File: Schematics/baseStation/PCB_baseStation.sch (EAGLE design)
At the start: 9 parts, among them U1 ATMEGA328P, U2 MCP1824ST-3302E/DB

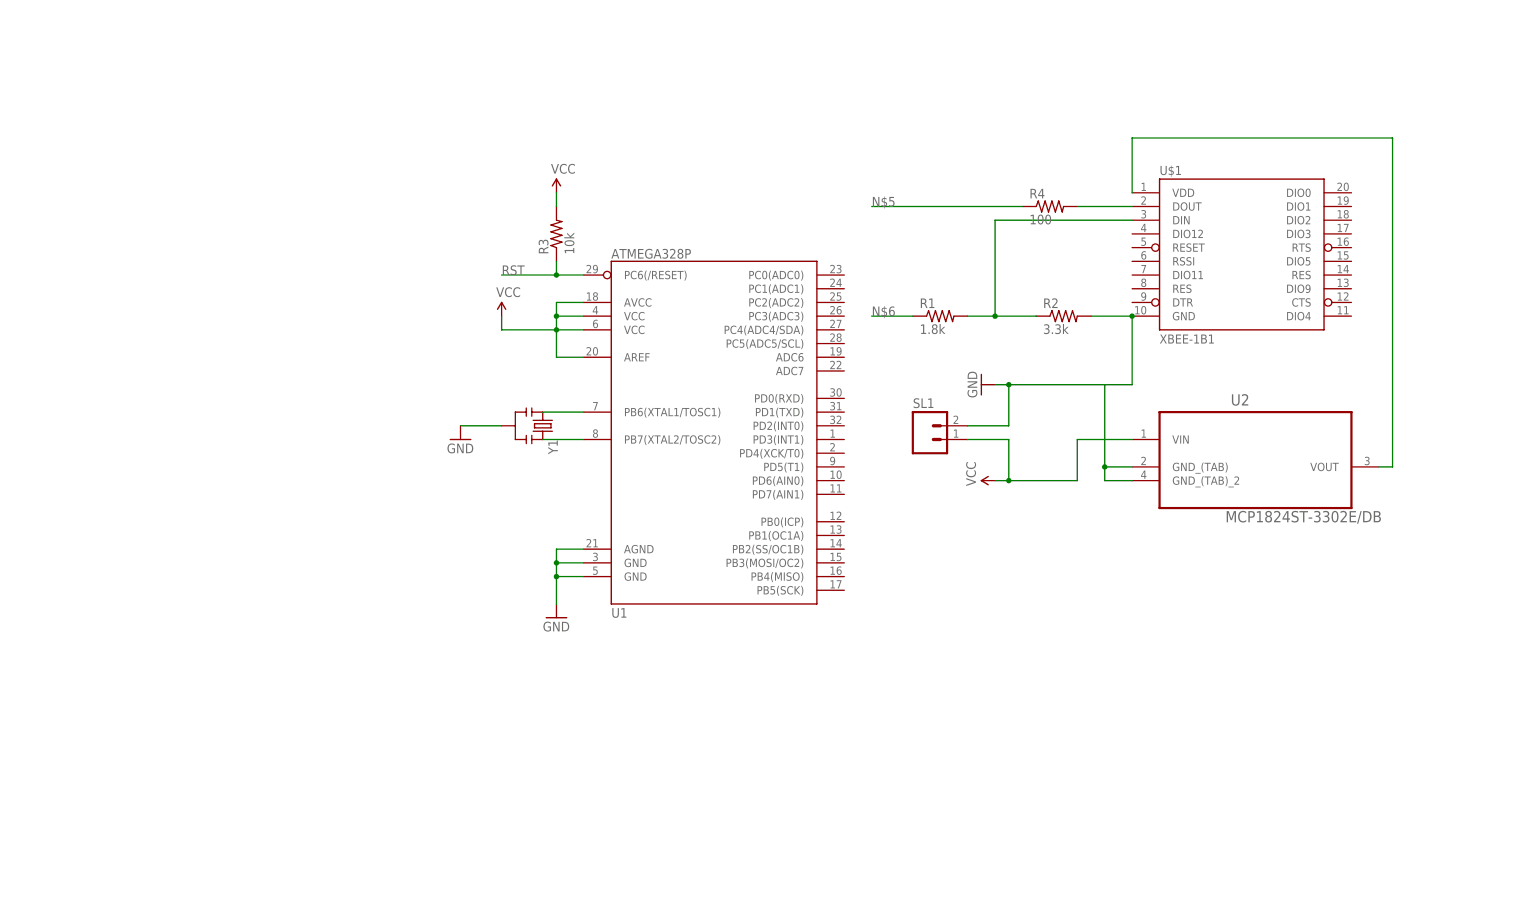
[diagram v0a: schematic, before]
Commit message: Base Station PCB 1.0
Finished Base Station PCB design version 1.0
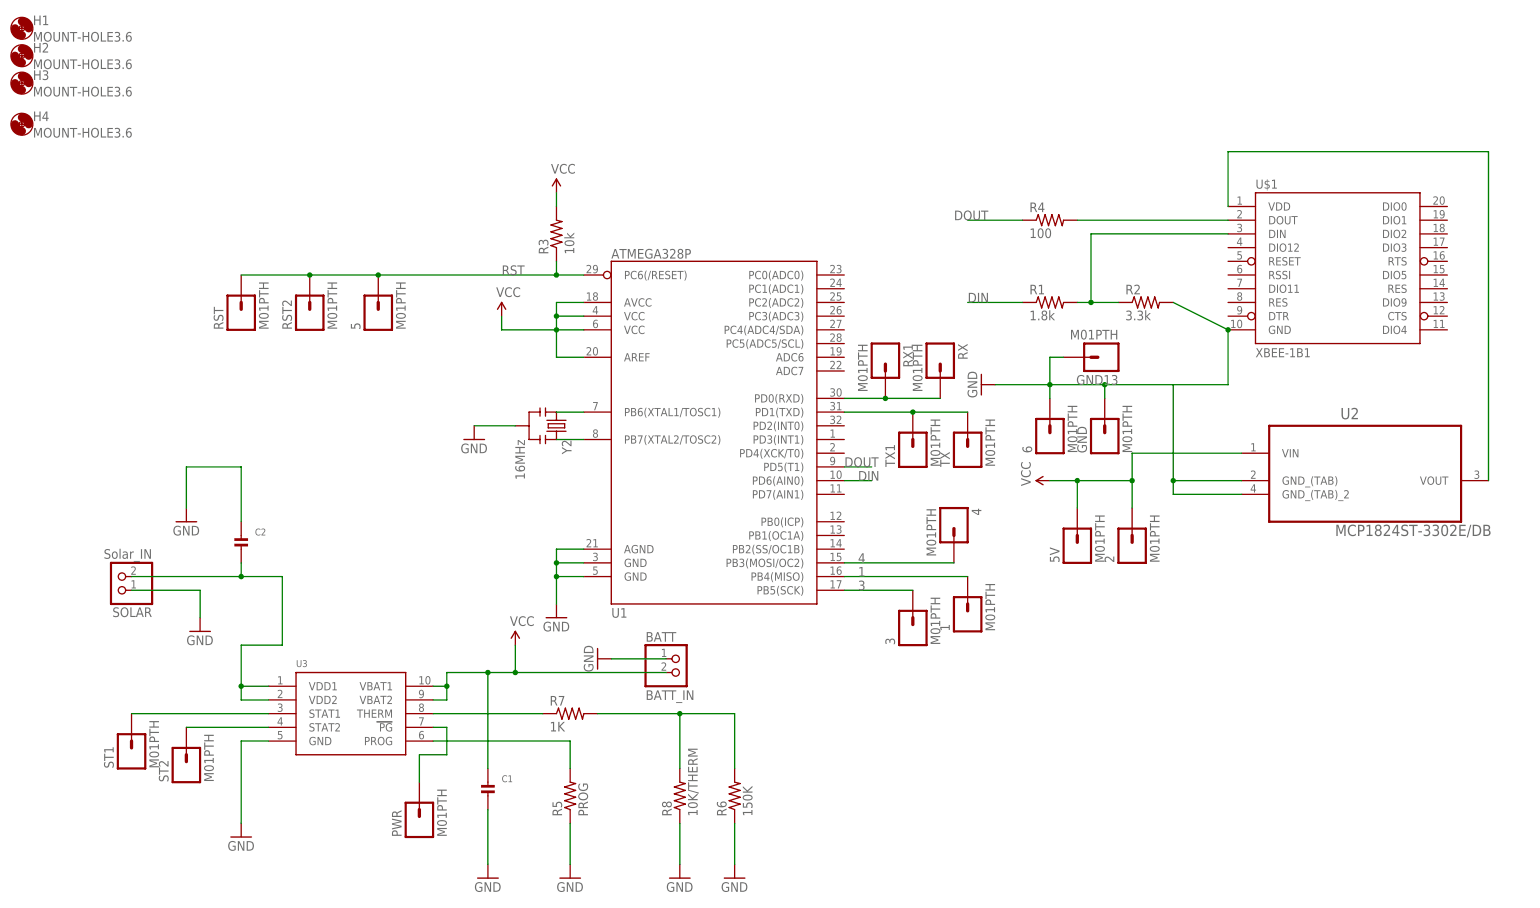
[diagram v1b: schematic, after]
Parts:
- removed SL1: (no value), con-amp-quick:M02
- removed Y1: (no value), SparkFun-FreqCtrl:RESONATORPTH
- added 1, 2, 3, 4, 5, 5V, 6, GND, GND13, PWR, RST, RST2, RX, RX1, ST1, ST2, TX, TX1: M01PTH, SparkFun-Connectors:M01PTH
- added BATT: BATT_IN, microbuilder:JST_2PIN
- added C1, C2: (no value), microbuilder:CAP_CERAMIC0805
- added H1, H2, H3, H4: MOUNT-HOLE3.6, holes:MOUNT-HOLE3.6
- added R5: PROG, microbuilder:RESISTOR_DUAL
- added R6: 150K, adafruit:R-US_M0805
- added R7: 1K, adafruit:R-US_M0805
- added R8: 10K/THERM, adafruit:R-US_FLIPFLOP
- added SOLAR: Solar_IN, microbuilder:JST_2PIN
- added U3: (no value), microbuilder:MCP73833
- added Y2: 16MHz, SparkFun-FreqCtrl:RESONATOR16MHZ
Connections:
- removed net N$5: R4.1
- removed net N$6: R1.1
- new net 1: 1.1, U1.PB4(MISO)
- new net 3: 3.1, U1.PB5(SCK)
- new net 4: 4.1, U1.PB3(MOSI/OC2)
- new net DIN: R1.1, U1.PD6(AIN0)
- new net DOUT: R4.1, U1.PD5(T1)
- new net N$1: ST1.1, U3.STAT1
- new net N$10: R5.2, U3.PROG
- new net N$11: PWR.1, U3.PG
- new net N$13: R6.2, R7.2, R8.2
- new net N$15: R7.1, U3.THERM
- new net N$19: TX.1, TX1.1, U1.PD1(TXD)
- new net N$2: ST2.1, U3.STAT2
- new net N$20: RX.1, RX1.1, U1.PD0(RXD)
- new net N$9: C2.P$2, SOLAR.2, U3.VDD1, U3.VDD2
- net GND: now also 6.1, BATT.1, C1.P$2, C2.P$1, GND.1, GND13.1, R5.1, R6.1, R8.1, SOLAR.1, U3.GND, Y2.2; no longer SL1.2, Y1.2
- net N$7: now also Y2.1; no longer Y1.1
- net N$8: now also Y2.3; no longer Y1.3
- net RST: now also 5.1, RST.1, RST2.1
- net VCC: now also 2.1, 5V.1, BATT.2, C1.P$1, U3.VBAT1, U3.VBAT2; no longer SL1.1
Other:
- moved on the sheet: R1, R2, R4, U$1, U2

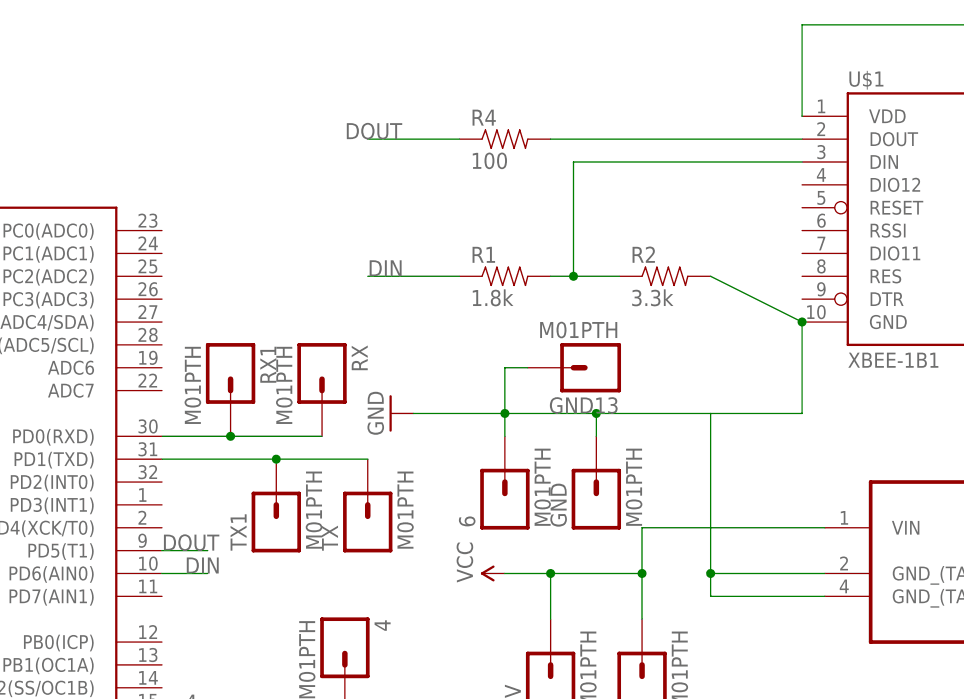
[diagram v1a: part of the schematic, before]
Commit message: Base Station PCB improvements
Base_SP 1.1
moved prop plug and ISP closer in
added two resistors to limit voltage from arduino to xbee pin 9(SLP)
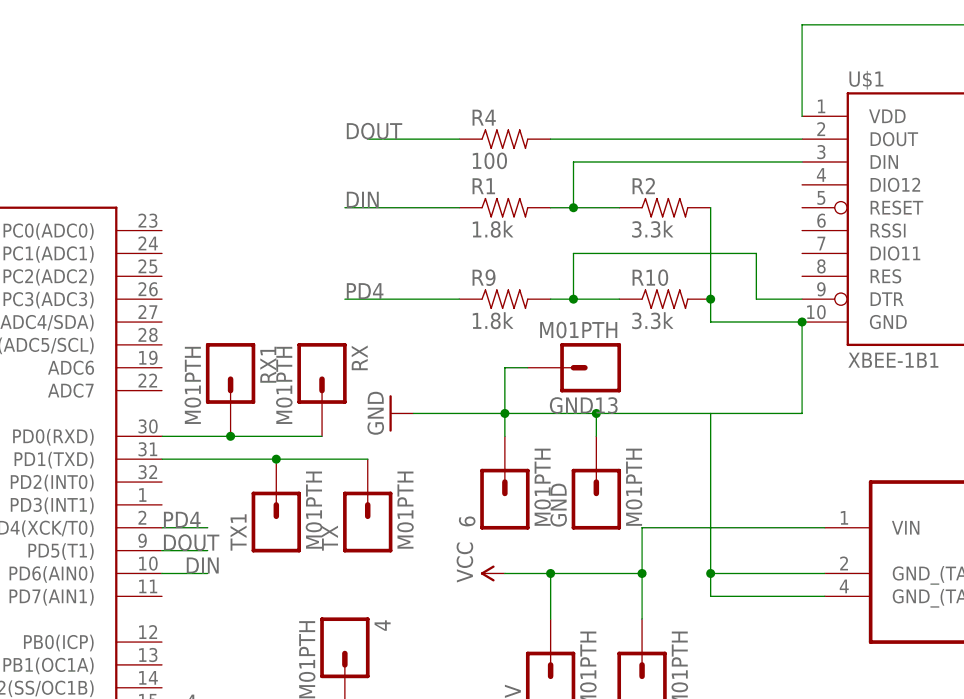
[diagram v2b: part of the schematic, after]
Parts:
- added R10: 3.3k, SparkFun-Resistors:3.3KOHM1/10W1%(0603)
- added R9: 1.8k, SparkFun-Resistors:1.8KOHM1/10W1%(0603)
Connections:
- new net N$6: R10.1, R9.2, U$1.DTR
- new net PD4: R9.1, U1.PD4(XCK/T0)
- net GND: now also R10.2
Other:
- moved on the sheet: R1, R2
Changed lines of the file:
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@@
 <part name="GND13" library="SparkFun-Connectors" deviceset="M01" device="PTH"/>
 <part name="RST2" library="SparkFun-Connectors" deviceset="M01" device="PTH"/>
+<part name="R9" library="SparkFun-Resistors" deviceset="1.8KOHM1/10W1%(0603)" device="" value="1.8k"/>
+<part name="R10" library="SparkFun-Resistors" deviceset="3.3KOHM1/10W1%(0603)" device="" value="3.3k"/>
 </parts>
 <sheets>
@@
 <instance part="U1" gate="G$1" x="5.08" y="48.26"/>
 <instance part="U$1" gate="G$1" x="121.92" y="76.2"/>
-<instance part="R1" gate="G$1" x="68.58" y="68.58"/>
-<instance part="R2" gate="G$1" x="86.36" y="68.58"/>
+<instance part="R1" gate="G$1" x="68.58" y="76.2"/>
+<instance part="R2" gate="G$1" x="86.36" y="76.2"/>
 <instance part="R3" gate="G$1" x="-22.86" y="81.28" rot="R90"/>
 <instance part="R4" gate="G$1" x="68.58" y="83.82"/>
@@
 <instance part="GND13" gate="G$1" x="78.74" y="58.42" rot="R180"/>
 <instance part="RST2" gate="G$1" x="-68.58" y="66.04" rot="R90"/>
+<instance part="R9" gate="G$1" x="68.58" y="66.04"/>
+<instance part="R10" gate="G$1" x="86.36" y="66.04"/>
 </instances>
 <busses>
@@
 <pinref part="R2" gate="G$1" pin="1"/>
 <pinref part="R1" gate="G$1" pin="2"/>
-<wire x1="81.28" y1="68.58" x2="76.2" y2="68.58" width="0.1524" layer="91"/>
-<wire x1="76.2" y1="68.58" x2="73.66" y2="68.58" width="0.1524" layer="91"/>
-<wire x1="76.2" y1="68.58" x2="76.2" y2="81.28" width="0.1524" layer="91"/>
-<junction x="76.2" y="68.58"/>
+<wire x1="81.28" y1="76.2" x2="76.2" y2="76.2" width="0.1524" layer="91"/>
+<wire x1="76.2" y1="76.2" x2="73.66" y2="76.2" width="0.1524" layer="91"/>
+<wire x1="76.2" y1="76.2" x2="76.2" y2="81.28" width="0.1524" layer="91"/>
+<junction x="76.2" y="76.2"/>
 <pinref part="U$1" gate="G$1" pin="DIN"/>
 <wire x1="76.2" y1="81.28" x2="101.6" y2="81.28" width="0.1524" layer="91"/>
@@
 <segment>
 <pinref part="R1" gate="G$1" pin="1"/>
-<wire x1="63.5" y1="68.58" x2="53.34" y2="68.58" width="0.1524" layer="91"/>
-<label x="53.34" y="68.58" size="1.778" layer="95"/>
+<wire x1="63.5" y1="76.2" x2="50.8" y2="76.2" width="0.1524" layer="91"/>
+<label x="50.8" y="76.2" size="1.778" layer="95"/>
 </segment>
 <segment>
@@
 </segment>
 <segment>
-<pinref part="R2" gate="G$1" pin="2"/>
 <pinref part="U$1" gate="G$1" pin="GND"/>
-<wire x1="91.44" y1="68.58" x2="101.6" y2="63.5" width="0.1524" layer="91"/>
 <wire x1="101.6" y1="63.5" x2="101.6" y2="53.34" width="0.1524" layer="91"/>
-<junction x="101.6" y="63.5"/>
 <wire x1="101.6" y1="53.34" x2="78.74" y2="53.34" width="0.1524" layer="91"/>
 <pinref part="GND1" gate="1" pin="GND"/>
@@
 <wire x1="71.12" y1="58.42" x2="68.58" y2="58.42" width="0.1524" layer="91"/>
 <wire x1="68.58" y1="58.42" x2="68.58" y2="53.34" width="0.1524" layer="91"/>
+<wire x1="101.6" y1="63.5" x2="91.44" y2="63.5" width="0.1524" layer="91"/>
+<junction x="101.6" y="63.5"/>
+<pinref part="R2" gate="G$1" pin="2"/>
+<wire x1="91.44" y1="63.5" x2="91.44" y2="66.04" width="0.1524" layer="91"/>
+<pinref part="R10" gate="G$1" pin="2"/>
+<wire x1="91.44" y1="66.04" x2="91.44" y2="76.2" width="0.1524" layer="91"/>
+<junction x="91.44" y="66.04"/>
 </segment>
 <segment>
@@
 </segment>
 </net>
+<net name="PD4" class="0">
+<segment>
+<pinref part="U1" gate="G$1" pin="PD4(XCK/T0)"/>
+<wire x1="30.48" y1="40.64" x2="35.56" y2="40.64" width="0.1524" layer="91"/>
+<label x="30.48" y="40.64" size="1.778" layer="95"/>
+</segment>
+<segment>
+<pinref part="R9" gate="G$1" pin="1"/>
+<wire x1="63.5" y1="66.04" x2="50.8" y2="66.04" width="0.1524" layer="91"/>
+<label x="50.8" y="66.04" size="1.778" layer="95"/>
+</segment>
+</net>
+<net name="N$6" class="0">
+<segment>
+<pinref part="R9" gate="G$1" pin="2"/>
+<pinref part="R10" gate="G$1" pin="1"/>
+<wire x1="73.66" y1="66.04" x2="76.2" y2="66.04" width="0.1524" layer="91"/>
+<pinref part="U$1" gate="G$1" pin="DTR"/>
+<wire x1="76.2" y1="66.04" x2="81.28" y2="66.04" width="0.1524" layer="91"/>
+<wire x1="101.6" y1="66.04" x2="96.52" y2="66.04" width="0.1524" layer="91"/>
+<wire x1="96.52" y1="66.04" x2="96.52" y2="71.12" width="0.1524" layer="91"/>
+<wire x1="96.52" y1="71.12" x2="76.2" y2="71.12" width="0.1524" layer="91"/>
+<wire x1="76.2" y1="71.12" x2="76.2" y2="66.04" width="0.1524" layer="91"/>
+<junction x="76.2" y="66.04"/>
+</segment>
+</net>

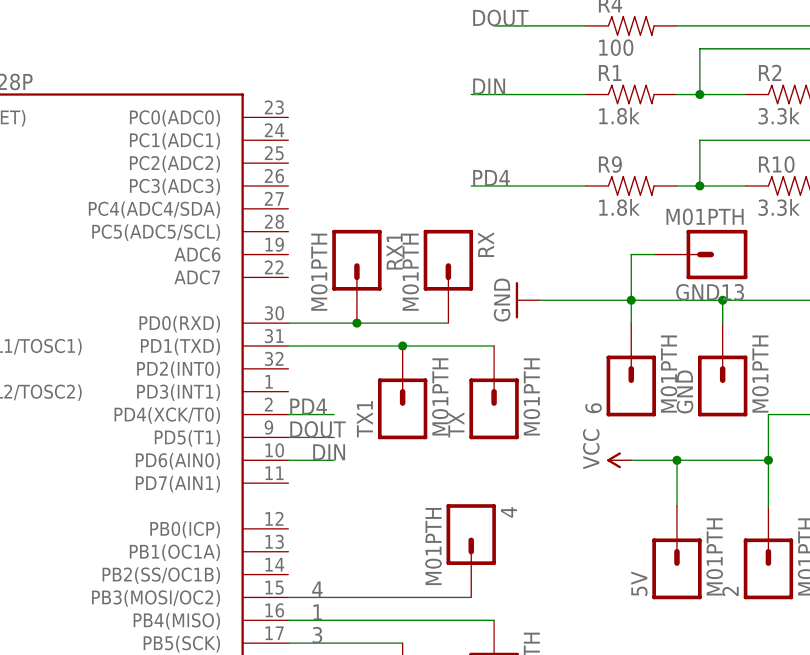
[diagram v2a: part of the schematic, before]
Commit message: Base Station PCB Improvements
Base_SP 1.2
moved components around to group them better
corrected xbee pin 9 to be connected from arduino PD4 to PD7
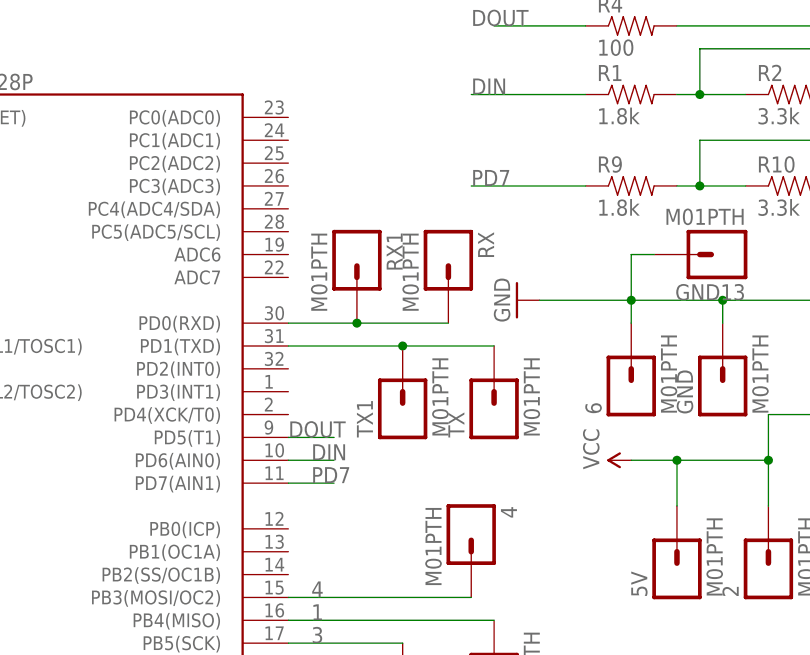
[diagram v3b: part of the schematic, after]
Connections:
- removed net PD4: R9.1, U1.PD4(XCK/T0)
- new net PD7: R9.1, U1.PD7(AIN1)
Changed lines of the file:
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@@
-</segment>
-</net>
-<net name="PD4" class="0">
-<segment>
-<pinref part="U1" gate="G$1" pin="PD4(XCK/T0)"/>
-<wire x1="30.48" y1="40.64" x2="35.56" y2="40.64" width="0.1524" layer="91"/>
-<label x="30.48" y="40.64" size="1.778" layer="95"/>
-</segment>
-<segment>
-<pinref part="R9" gate="G$1" pin="1"/>
-<wire x1="63.5" y1="66.04" x2="50.8" y2="66.04" width="0.1524" layer="91"/>
-<label x="50.8" y="66.04" size="1.778" layer="95"/>
 </segment>
 </net>
@@
 </segment>
 </net>
+<net name="PD7" class="0">
+<segment>
+<pinref part="U1" gate="G$1" pin="PD7(AIN1)"/>
+<wire x1="30.48" y1="33.02" x2="35.56" y2="33.02" width="0.1524" layer="91"/>
+<label x="33.02" y="33.02" size="1.778" layer="95"/>
+</segment>
+<segment>
+<pinref part="R9" gate="G$1" pin="1"/>
+<wire x1="63.5" y1="66.04" x2="50.8" y2="66.04" width="0.1524" layer="91"/>
+<label x="50.8" y="66.04" size="1.778" layer="95"/>
+</segment>
+</net>
